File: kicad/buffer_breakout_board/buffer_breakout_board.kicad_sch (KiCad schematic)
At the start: 46 parts, among them J1 Power, J2 Vcca_select, J3 In_Hi, J4 In_Lo, J5 Out_Hi, J6 Out_Lo, J7 Vccb_select, J8 JST_SH_BM04B-SRSS-TB, J9 Signals, U1 MCP4725A2T-E/CH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

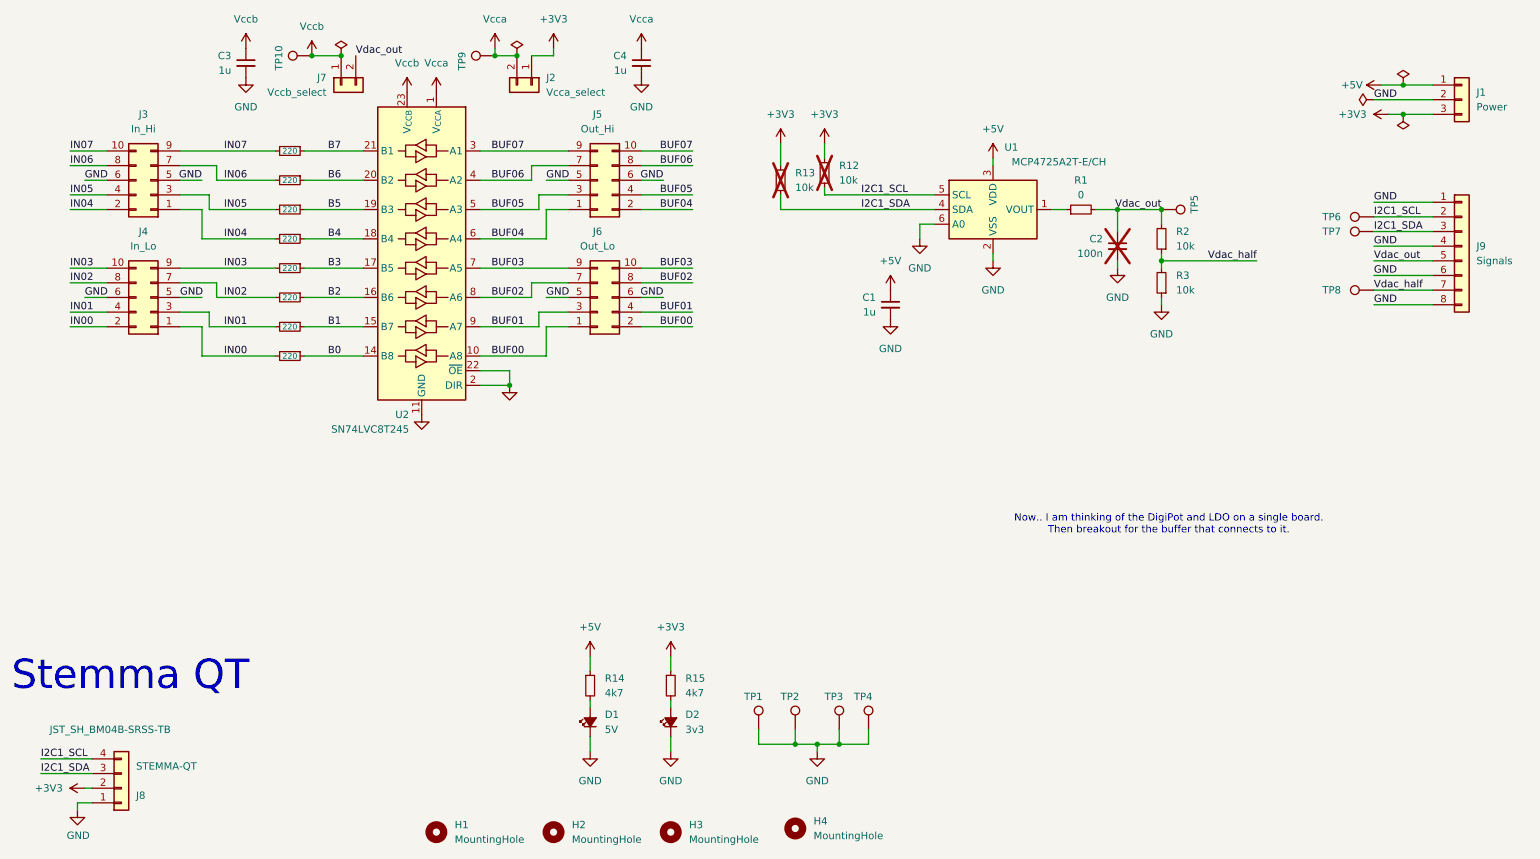
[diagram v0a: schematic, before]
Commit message: renamed files, was working on wrong directory
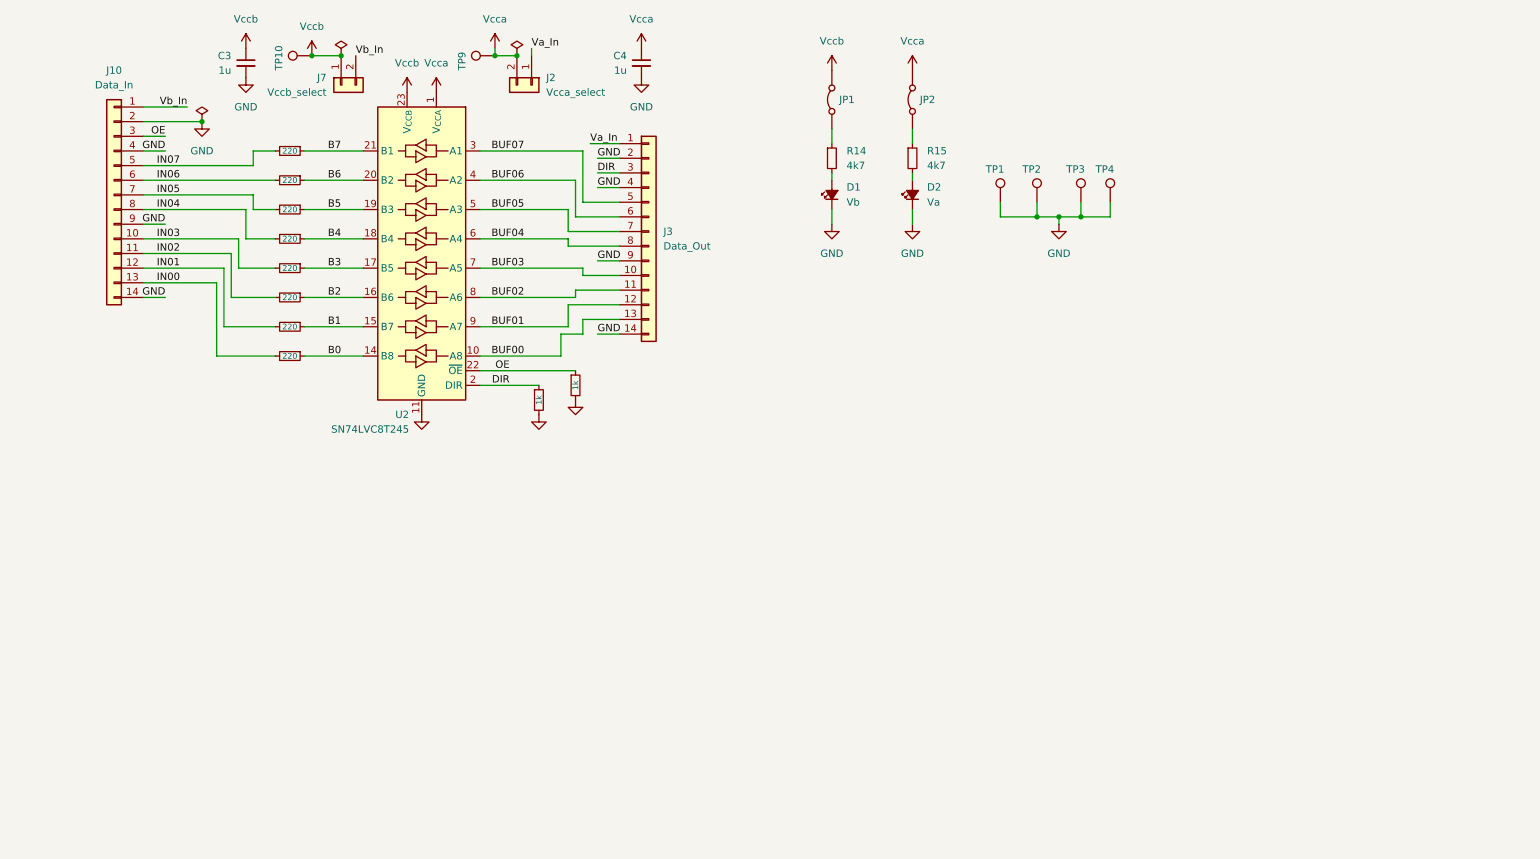
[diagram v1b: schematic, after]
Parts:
- removed C1: 1u, Capacitor_SMD:C_0603_1608Metric_Pad1.08x0.95mm_HandSolder, symbol Device:C_Small
- removed C2: 100n, Capacitor_SMD:C_0603_1608Metric_Pad1.08x0.95mm_HandSolder, symbol Device:C_Small
- removed H1, H2, H3, H4: MountingHole, MountingHole:MountingHole_2.7mm, symbol Mechanical:MountingHole
- removed J1: Power, Connector_PinHeader_2.54mm:PinHeader_1x03_P2.54mm_Vertical, symbol Connector_Generic:Conn_01x03
- removed J3: In_Hi, Connector_PinHeader_2.54mm:PinHeader_2x05_P2.54mm_Vertical, symbol Connector_Generic:Conn_02x05_Odd_Even
- removed J4: In_Lo, Connector_PinHeader_2.54mm:PinHeader_2x05_P2.54mm_Vertical, symbol Connector_Generic:Conn_02x05_Odd_Even
- removed J5: Out_Hi, Connector_PinHeader_2.54mm:PinHeader_2x05_P2.54mm_Vertical, symbol Connector_Generic:Conn_02x05_Odd_Even
- removed J6: Out_Lo, Connector_PinHeader_2.54mm:PinHeader_2x05_P2.54mm_Vertical, symbol Connector_Generic:Conn_02x05_Odd_Even
- removed J8: JST_SH_BM04B-SRSS-TB, Connector_JST:JST_SH_BM04B-SRSS-TB_1x04-1MP_P1.00mm_Vertical, symbol Connector_Generic:Conn_01x04
- removed J9: Signals, Connector_PinHeader_2.54mm:PinHeader_1x08_P2.54mm_Vertical, symbol Connector_Generic:Conn_01x08
- removed R12, R13, R3: 10k, Resistor_SMD:R_0603_1608Metric, symbol Device:R_Small
- removed TP5, TP6, TP7, TP8: TestPoint_Harwin, My Libraries:Harwin-S1751-46-Test-Point, symbol My Library:TestPoint_Harwin
- removed U1: MCP4725A2T-E/CH, Package_TO_SOT_SMD:SOT-23-6, symbol Analog_DAC:MCP4725xxx-xCH
- added J10: Data_In, Connector_PinHeader_2.54mm:PinHeader_1x14_P2.54mm_Vertical, symbol Connector_Generic:Conn_01x14
- added J3: Data_Out, Connector_PinHeader_2.54mm:PinHeader_1x14_P2.54mm_Vertical, symbol Connector_Generic:Conn_01x14
- added JP1, JP2: Jumper_2_Bridged, Jumper:SolderJumper-2_P1.3mm_Bridged_RoundedPad1.0x1.5mm, symbol Jumper:Jumper_2_Bridged
- D1: value 5V -> Vb
- D2: value 3v3 -> Va
- R1: value 0 -> 1k
- R2: value 10k -> 1k
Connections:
- net BUF00: now also J3.13 (Pin_13)
- net BUF01: now also J3.12 (Pin_12)
- net BUF02: now also J3.11 (Pin_11)
- net BUF03: now also J3.10 (Pin_10)
- net BUF04: now also J3.8 (Pin_8)
- net BUF05: now also J3.7 (Pin_7)
- net BUF06: now also J3.6 (Pin_6)
- net BUF07: now also J3.5 (Pin_5)
- net GND: now also R1.2, R2.2, J10.14 (Pin_14), J10.2 (Pin_2), J10.4 (Pin_4), J10.9 (Pin_9), J3.14 (Pin_14), J3.2 (Pin_2), J3.4 (Pin_4), J3.9 (Pin_9); no longer U2.2 (DIR), U2.22 (~{OE})
- net IN00: now also J10.13 (Pin_13)
- net IN01: now also J10.12 (Pin_12)
- net IN02: now also J10.11 (Pin_11)
- net IN03: now also J10.10 (Pin_10)
- net IN04: now also J10.8 (Pin_8)
- net IN05: now also J10.7 (Pin_7)
- net IN06: now also J10.6 (Pin_6)
- net IN07: now also J10.5 (Pin_5)
- net Vcca: now also JP2.2 (B)
- net Vccb: now also JP1.2 (B)
- net DIR: now reaches R1.1
- net DIR: now also U2.2 (DIR), J3.3 (Pin_3)
- net +3V3: no longer names the net of R15.1
- net +3V3: now also JP2.1 (A); no longer J2.1 (Pin_1)
- net +5V: no longer names the net of R14.1
- net +5V: now also JP1.1 (A)
- net Vdac_half renamed OE
- net OE: now also U2.22 (~{OE}), J10.3 (Pin_3)
- removed net Vdac_out: J7.2 (Pin_2), R1.2, R2.2
- new net Va_In: J2.1 (Pin_1), J3.1 (Pin_1)
- new net Vb_In: J10.1 (Pin_1), J7.2 (Pin_2)
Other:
- note removed: "Now.. I am thinking of the DigiPot and LDO on a single board. Then breakout for the buffer that connects to it."
- note removed: "Stemma QT"
- moved on the sheet: D1, D2, R14, R15, TP1, TP2, TP3, TP4

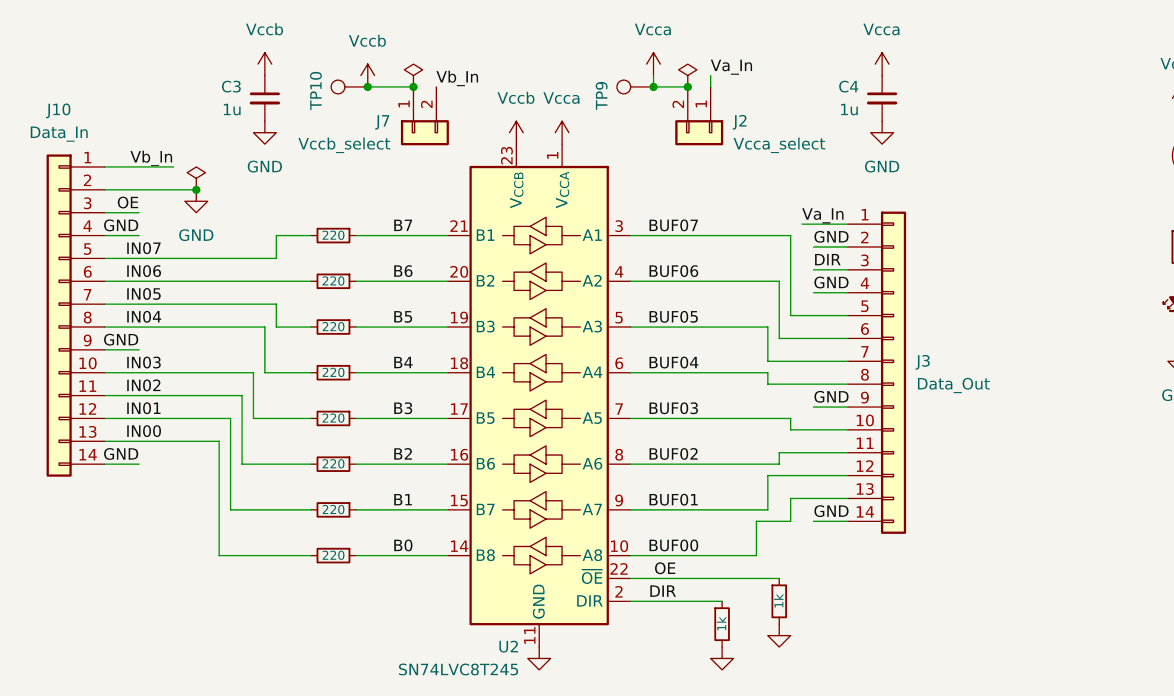
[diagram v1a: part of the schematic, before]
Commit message: floor planning attempt 1
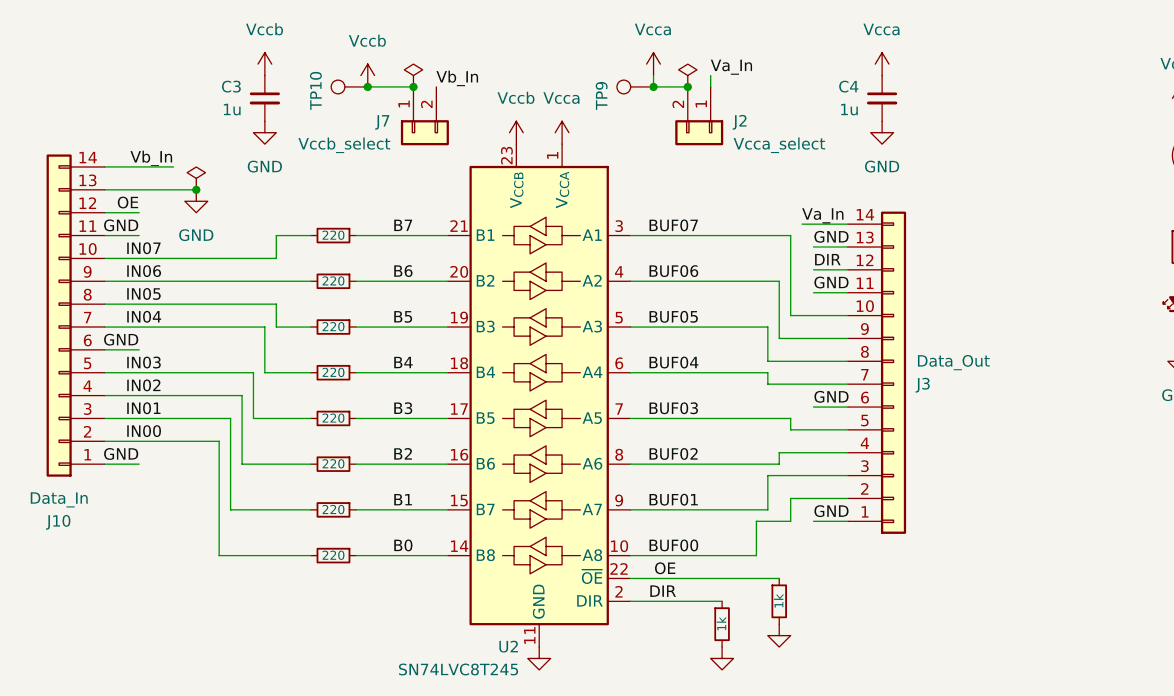
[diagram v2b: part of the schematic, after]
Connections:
- net BUF00: now also J3.2 (Pin_2); no longer J3.13 (Pin_13)
- net BUF01: now also J3.3 (Pin_3); no longer J3.12 (Pin_12)
- net BUF02: now also J3.4 (Pin_4); no longer J3.11 (Pin_11)
- net BUF03: now also J3.5 (Pin_5); no longer J3.10 (Pin_10)
- net BUF04: now also J3.7 (Pin_7); no longer J3.8 (Pin_8)
- net BUF05: now also J3.8 (Pin_8); no longer J3.7 (Pin_7)
- net BUF06: now also J3.9 (Pin_9); no longer J3.6 (Pin_6)
- net BUF07: now also J3.10 (Pin_10); no longer J3.5 (Pin_5)
- net DIR: now also J3.12 (Pin_12); no longer J3.3 (Pin_3)
- net GND: now also J10.1 (Pin_1), J10.11 (Pin_11), J10.13 (Pin_13), J10.6 (Pin_6), J3.1 (Pin_1), J3.11 (Pin_11), J3.13 (Pin_13), J3.6 (Pin_6); no longer J10.14 (Pin_14), J10.2 (Pin_2), J10.4 (Pin_4), J10.9 (Pin_9), J3.14 (Pin_14), J3.2 (Pin_2), J3.4 (Pin_4), J3.9 (Pin_9)
- net IN00: now also J10.2 (Pin_2); no longer J10.13 (Pin_13)
- net IN01: now also J10.3 (Pin_3); no longer J10.12 (Pin_12)
- net IN02: now also J10.4 (Pin_4); no longer J10.11 (Pin_11)
- net IN03: now also J10.5 (Pin_5); no longer J10.10 (Pin_10)
- net IN04: now also J10.7 (Pin_7); no longer J10.8 (Pin_8)
- net IN05: now also J10.8 (Pin_8); no longer J10.7 (Pin_7)
- net IN06: now also J10.9 (Pin_9); no longer J10.6 (Pin_6)
- net IN07: now also J10.10 (Pin_10); no longer J10.5 (Pin_5)
- net OE: now also J10.12 (Pin_12); no longer J10.3 (Pin_3)
- net Va_In: now also J3.14 (Pin_14); no longer J3.1 (Pin_1)
- net Vb_In: now also J10.14 (Pin_14); no longer J10.1 (Pin_1)
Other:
- moved on the sheet: J10
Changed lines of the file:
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@@
 	(symbol
 		(lib_id "Connector_Generic:Conn_01x14")
-		(at 35.56 80.01 0)
-		(mirror y)
-		(unit 1)
-		(exclude_from_sim no)
-		(in_bom yes)
-		(on_board yes)
-		(dnp no)
-		(fields_autoplaced yes)
+		(at 35.56 82.55 180)
+		(unit 1)
+		(exclude_from_sim no)
+		(in_bom yes)
+		(on_board yes)
+		(dnp no)
 		(property "Reference" "J10"
-			(at 35.56 58.42 0)
+			(at 35.56 104.14 0)
 			(effects
 				(font
@@
 		)
 		(property "Value" "Data_In"
-			(at 35.56 60.96 0)
+			(at 35.56 101.6 0)
 			(effects
 				(font
@@
 		)
 		(property "Footprint" "Connector_PinHeader_2.54mm:PinHeader_1x14_P2.54mm_Vertical"
-			(at 35.56 80.01 0)
-			(effects
-				(font
-					(size 1.27 1.27)
-				)
-				(hide yes)
-			)
-		)
-		(property "Datasheet" "~"
-			(at 35.56 80.01 0)
+			(at 35.56 82.55 0)
+			(effects
+				(font
+					(size 1.27 1.27)
+				)
+				(hide yes)
+			)
+		)
+		(property "Datasheet" "~"
+			(at 35.56 82.55 0)
 			(effects
 				(font
@@
 		)
 		(property "Description" "Generic connector, single row, 01x14, script generated (kicad-library-utils/schlib/autogen/connector/)"
-			(at 35.56 80.01 0)
+			(at 35.56 82.55 0)
 			(effects
 				(font
@@
 	(symbol
 		(lib_id "Connector_Generic:Conn_01x14")
-		(at 128.27 86.36 0)
-		(unit 1)
-		(exclude_from_sim no)
-		(in_bom yes)
-		(on_board yes)
-		(dnp no)
-		(fields_autoplaced yes)
+		(at 128.27 88.9 0)
+		(mirror x)
+		(unit 1)
+		(exclude_from_sim no)
+		(in_bom yes)
+		(on_board yes)
+		(dnp no)
 		(property "Reference" "J3"
-			(at 130.81 86.3599 0)
+			(at 130.81 88.9001 0)
 			(effects
 				(font
@@
 		)
 		(property "Value" "Data_Out"
-			(at 130.81 88.8999 0)
+			(at 130.81 86.3601 0)
 			(effects
 				(font
@@
 		)
 		(property "Footprint" "Connector_PinHeader_2.54mm:PinHeader_1x14_P2.54mm_Vertical"
-			(at 128.27 86.36 0)
-			(effects
-				(font
-					(size 1.27 1.27)
-				)
-				(hide yes)
-			)
-		)
-		(property "Datasheet" "~"
-			(at 128.27 86.36 0)
+			(at 128.27 88.9 0)
+			(effects
+				(font
+					(size 1.27 1.27)
+				)
+				(hide yes)
+			)
+		)
+		(property "Datasheet" "~"
+			(at 128.27 88.9 0)
 			(effects
 				(font
@@
 		)
 		(property "Description" "Generic connector, single row, 01x14, script generated (kicad-library-utils/schlib/autogen/connector/)"
-			(at 128.27 86.36 0)
-			(effects
-				(font
+			(at 128.27 88.9 0)
+			(effects
+				(font

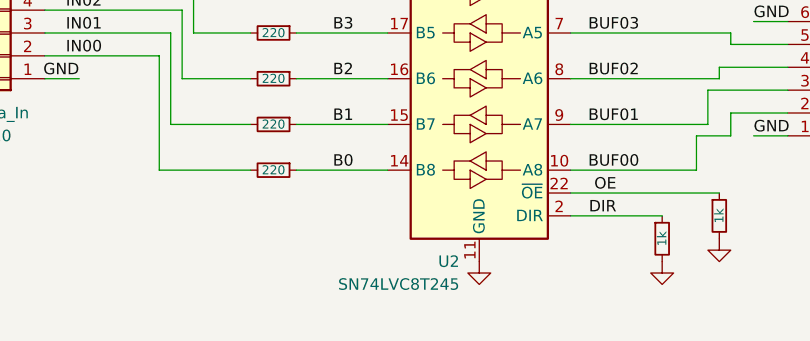
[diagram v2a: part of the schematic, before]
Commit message: generated BOMs for breakouts
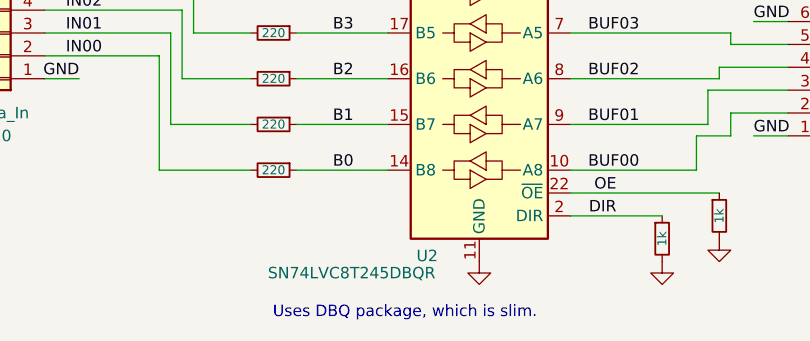
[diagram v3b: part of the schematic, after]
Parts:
- U2: value SN74LVC8T245 -> SN74LVC8T245DBQR
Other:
- note added: "Uses DBQ package, which is slim."
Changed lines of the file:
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@@
+		)
+	)
+	(text "Uses DBQ package, which is slim."
+		(exclude_from_sim no)
+		(at 80.645 123.825 0)
+		(effects
+			(font
+				(size 1.27 1.27)
+			)
 		)
 	)
@@
 		(on_board yes)
 		(dnp no)
-		(fields_autoplaced yes)
 		(property "Reference" "U2"
-			(at 86.7059 118.11 0)
-			(effects
-				(font
-					(size 1.27 1.27)
-				)
-				(justify left)
-			)
-		)
-		(property "Value" "SN74LVC8T245"
-			(at 86.7059 120.65 0)
-			(effects
-				(font
-					(size 1.27 1.27)
-				)
-				(justify left)
-			)
-		)
+			(at 81.915 117.475 0)
+			(effects
+				(font
+					(size 1.27 1.27)
+				)
+				(justify right)
+			)
+		)
+		(property "Value" "SN74LVC8T245DBQR"
+			(at 65.405 119.38 0)
+			(effects
+				(font
+					(size 1.27 1.27)
+				)
+				(justify right)
+			)
+		)
